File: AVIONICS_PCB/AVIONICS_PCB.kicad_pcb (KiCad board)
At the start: 2 copper layers, 5 parts, among them U1 ESP32-S3-DevKitC

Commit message: Added power system
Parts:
- added C1: C, Capacitor_SMD:C_0805_2012Metric_Pad1.18x1.45mm_HandSolder, F.Cu at (128.9, 81.0)
- added CR1: LD1117V33, LD1117V33:TO-220_STM, F.Cu at (131.5, 84.5)
- added J1: XT30PW-M, XT30PW-M:AMASS_XT30PW-M, F.Cu at (129.0, 66.7)
- moved SD_READER1 94.6 mm to (102.5, 119.0)
- moved GPS1 39.1 mm to (173.9, 66.0)
- moved ACCELEROMETER1 37.1 mm to (99.0, 80.7)
- moved ALTITUDE1 8.63 mm to (107.0, 89.2)
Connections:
- U1 pad 42: RX -> TX
- U1 pad 43: TX -> RX
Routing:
- net TX: track 0.00 -> 22.9 mm
- net RX: track 0.00 -> 20.9 mm
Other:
- board outline added: 103.5 x 77 mm

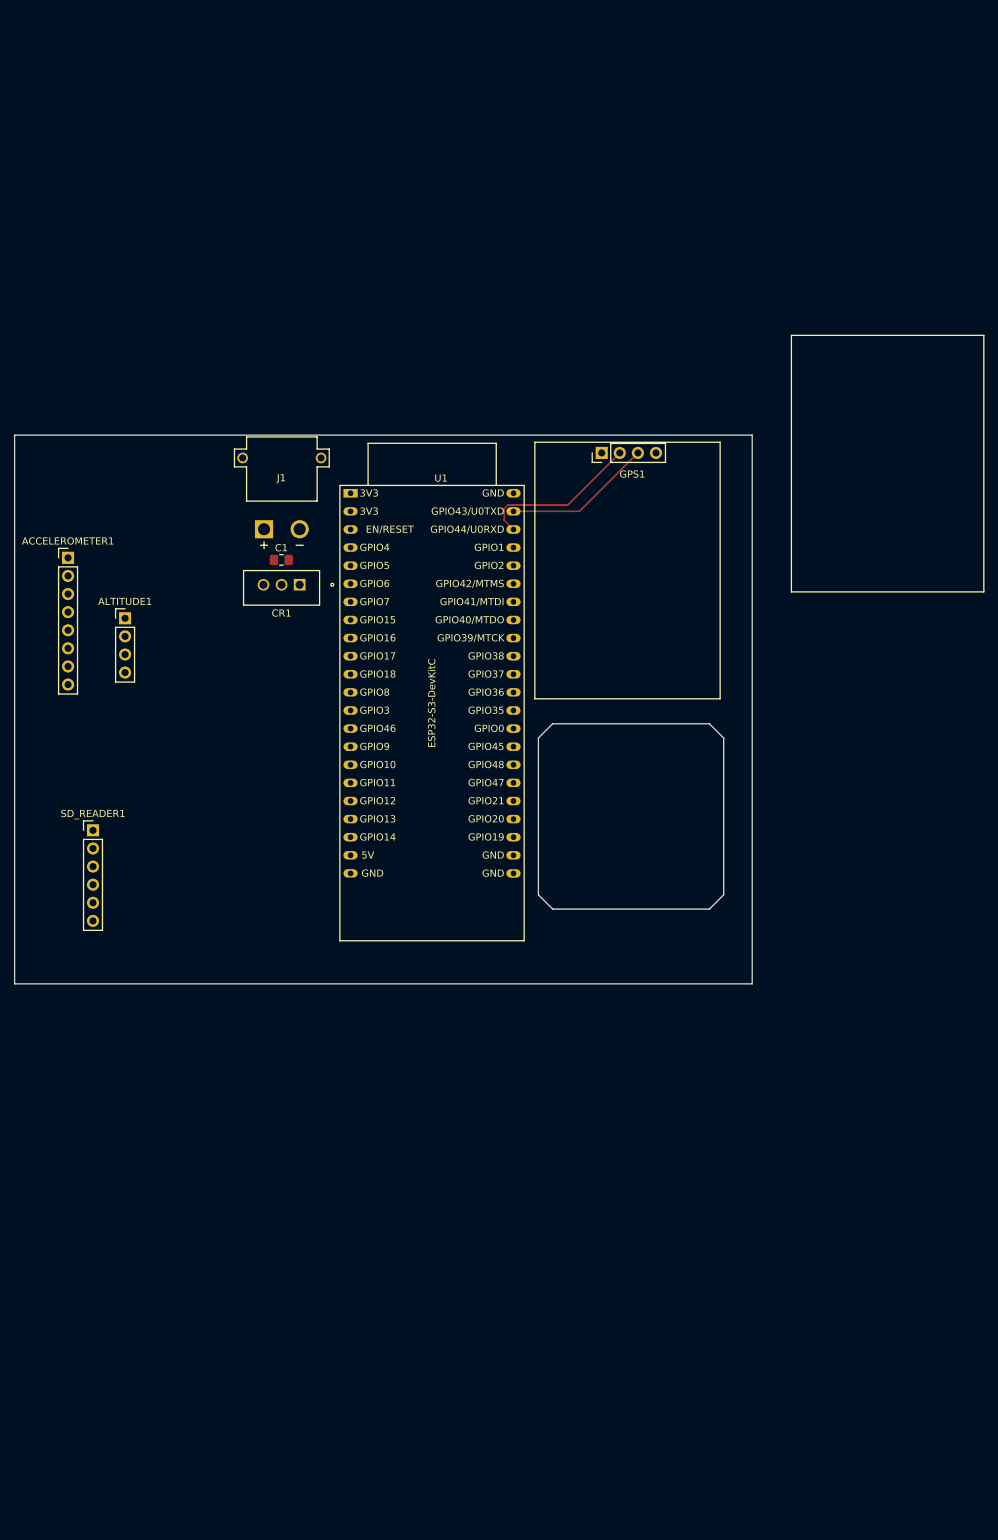
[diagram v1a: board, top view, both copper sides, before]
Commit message: Got sensors in right configuration
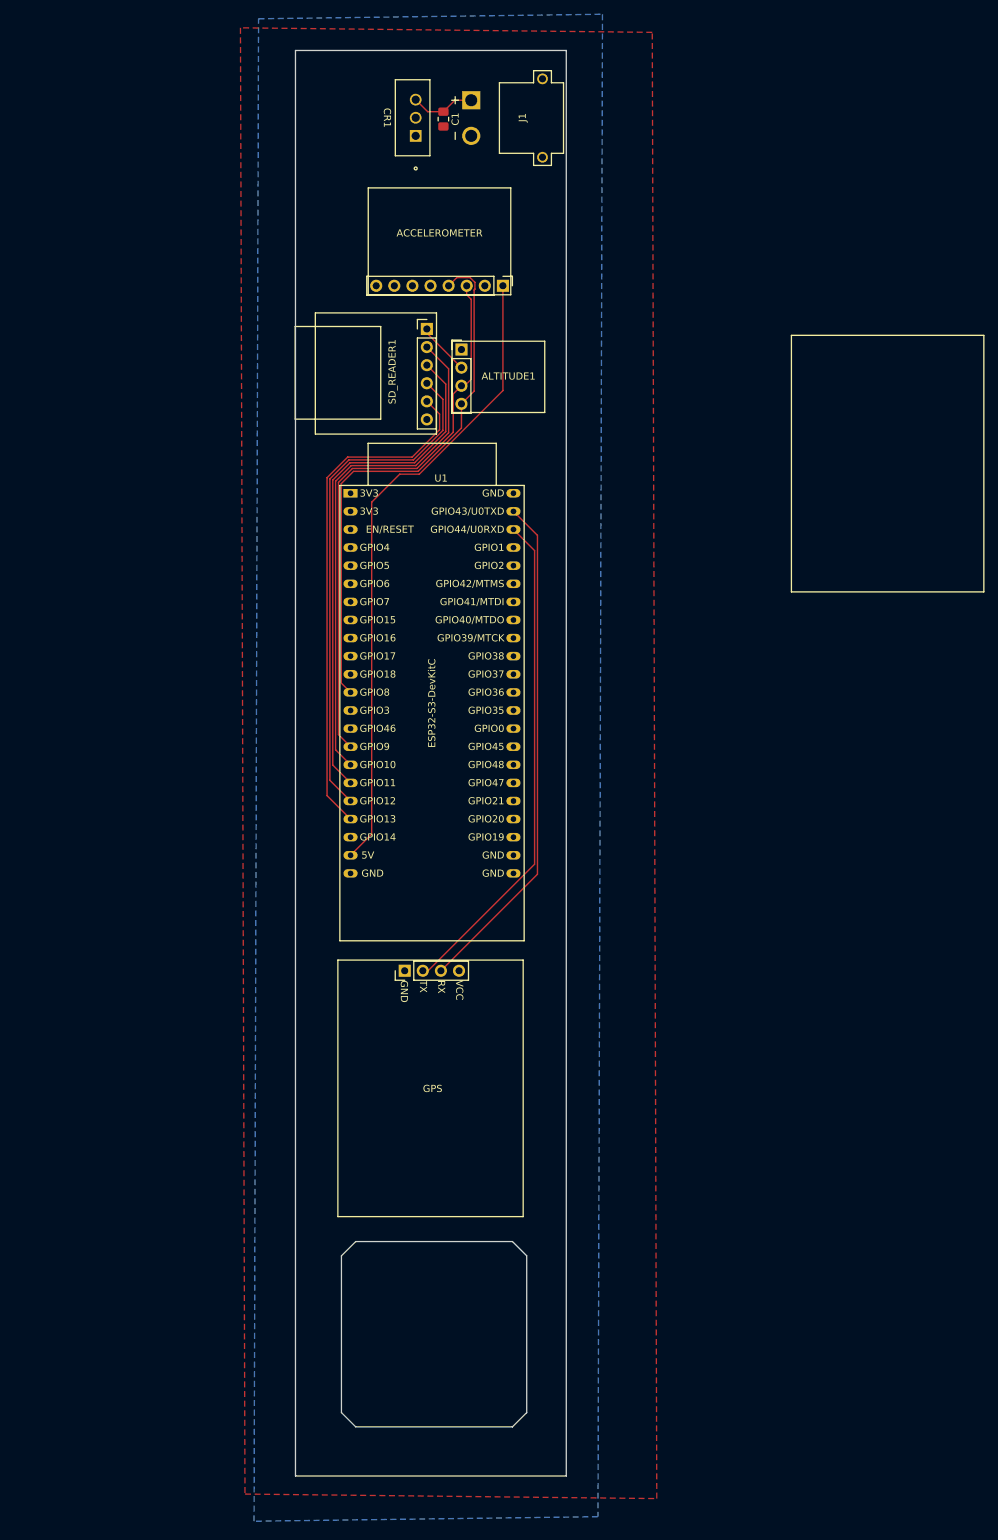
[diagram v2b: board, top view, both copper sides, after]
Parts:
- moved SD_READER1 84.5 mm to (149.3, 48.6)
- moved GPS 77.7 mm to (146.2, 138.7)
- moved ACCELEROMETER 72.0 mm to (160.0, 42.5), turned to -90 degrees
- moved C1 65.9 mm to (151.7, 19.2), turned to -90 degrees
- moved CR1 65.1 mm to (147.8, 21.5), turned to 90 degrees
- moved ALTITUDE1 60.4 mm to (154.2, 51.5)
- moved J1 60.1 mm to (165.6, 19.0), turned to -90 degrees
- renumbered ACCELEROMETER1 to ACCELEROMETER, GPS1 to GPS
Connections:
- GPS pad 4: +5V -> +3V3
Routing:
- net +5V: track 0.00 -> 90.4 mm
- net SCL: track 0.00 -> 78.9 mm
- net SDA: track 0.00 -> 75.6 mm
- net MOSI: track 0.00 -> 72.6 mm
- net CS: track 0.00 -> 72.6 mm
- net CLK: track 0.00 -> 72.6 mm
- net MISO: track 0.00 -> 72.6 mm
- net RX: track 20.9 -> 71.5 mm
- net TX: track 22.9 -> 70.1 mm
- net Net-(CR1-VIN): track 0.00 -> 9.16 mm
- net GND: track 0.00 -> 7.44 mm
- added copper zone on B.Cu, net +3V3
- added copper zone on F.Cu, net GND
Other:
- board size 103.5 x 77 mm -> 38 x 200 mm
- board text added: "GND"
- board text added: "RX"
- board text added: "TX"
- board text added: "VCC"

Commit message: Compact the board
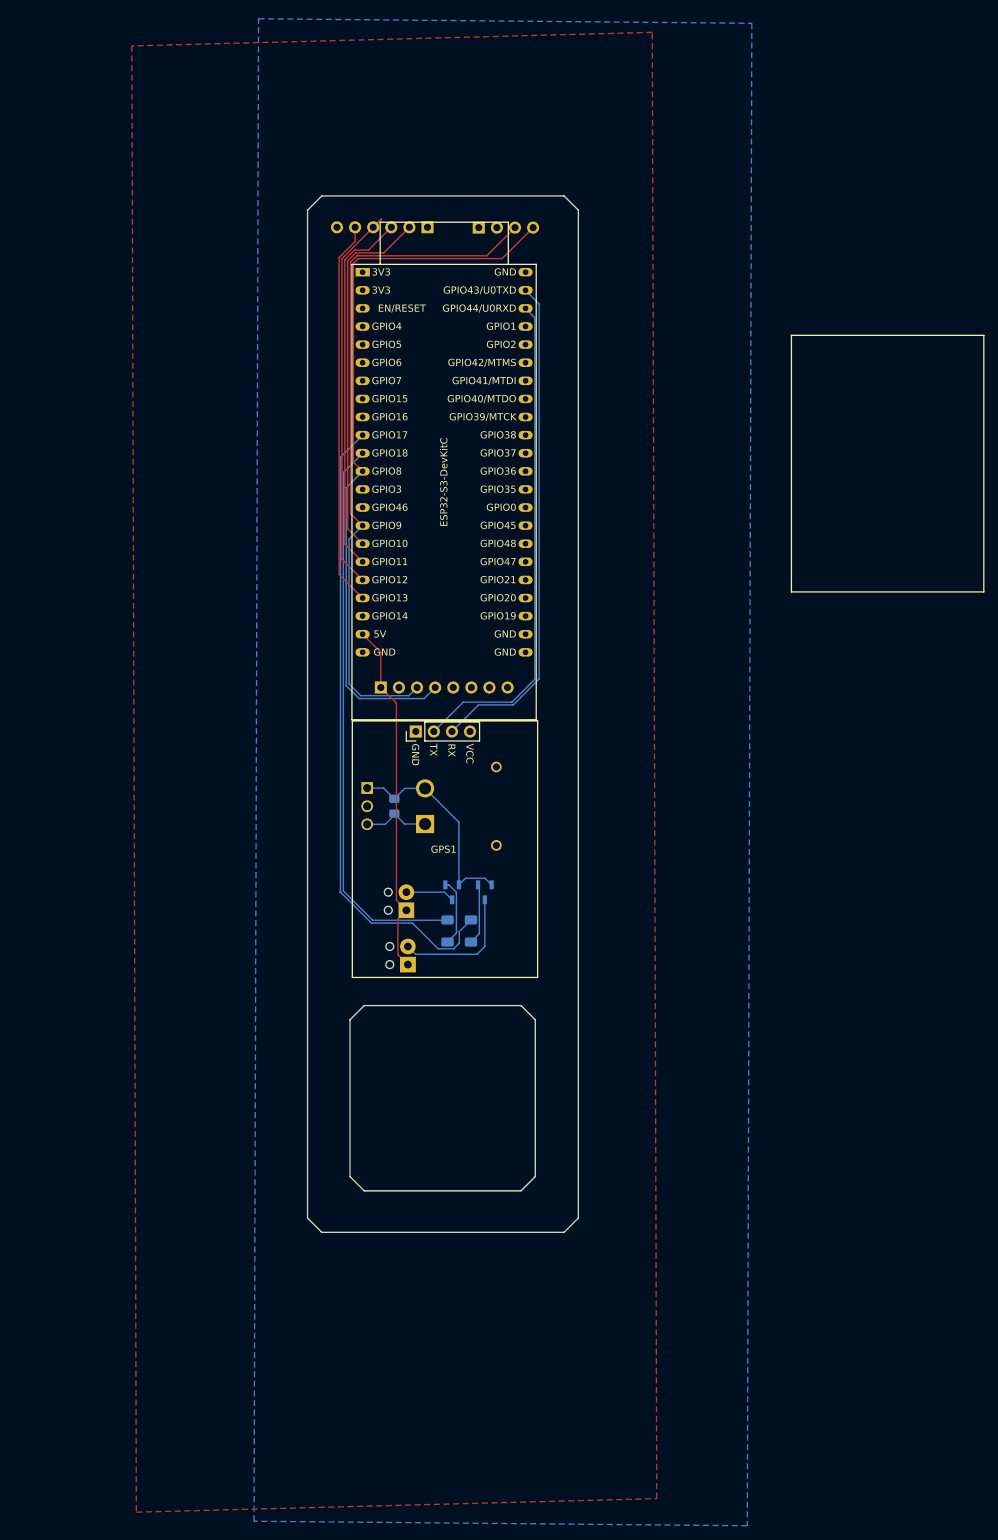
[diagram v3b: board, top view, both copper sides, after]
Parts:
- added IC1: MMBT2222ALT1G, SamacSys_Parts:SOT96P237X111-3N, B.Cu at (152.9, 127.7)
- added IC2: MMBT2222ALT1G, SamacSys_Parts:SOT96P237X111-3N, B.Cu at (157.5, 127.7)
- added J2: Screw_Terminal_01x02, TerminalBlock_Phoenix:TerminalBlock_Phoenix_MPT-0,5-2-2.54_1x02_P2.54mm_Horizontal, B.Cu at (146.5, 130.2)
- added J3: Screw_Terminal_01x02, TerminalBlock_Phoenix:TerminalBlock_Phoenix_MPT-0,5-2-2.54_1x02_P2.54mm_Horizontal, B.Cu at (146.7, 137.8)
- added R1: R_US, Resistor_SMD:R_1206_3216Metric_Pad1.30x1.75mm_HandSolder, B.Cu at (152.2, 133.1)
- added R2: R_US, Resistor_SMD:R_1206_3216Metric_Pad1.30x1.75mm_HandSolder, B.Cu at (155.5, 133.1)
- ACCELEROMETER1: renamed from ACCELEROMETER; moved to B.Cu
- ALTITUDE1, C1, CR1, J1, SD_READER1: moved to B.Cu
- moved J1 96.8 mm to (159.1, 115.6), turned to 90 degrees
- moved C1 96.7 mm to (144.8, 115.6), turned to 90 degrees
- moved CR1 91.8 mm to (141.0, 113.0), turned to -90 degrees
- moved ACCELEROMETER1 58.9 mm to (142.9, 98.9)
- moved GPS1 33.6 mm to (147.8, 105.1)
- moved U1 31.1 mm to (140.3, 40.6)
- moved ALTITUDE1 17.3 mm to (156.6, 34.4), turned to -90 degrees
- moved SD_READER1 14.3 mm to (149.4, 34.3), turned to 90 degrees
- renumbered GPS to GPS1
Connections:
- U1 pad 10: unconnected-(U1-GPIO17/ADC2_CH6-Pad10) -> Parachute2
- U1 pad 11: unconnected-(U1-GPIO18/ADC2_CH7-Pad11) -> Parachute1
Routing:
- net Parachute2: track 0.00 -> 89.7 mm
- net Parachute1: track 0.00 -> 78.9 mm
- net +5V: track 90.4 -> 50.0 mm
- net SDA: track 75.6 -> 101.9 mm
- net GND: track 7.44 -> 30.2 mm
- net CS: track 72.6 -> 51.2 mm
- net MOSI: track 72.6 -> 51.8 mm
- net Net-(IC2-C): track 0.00 -> 18.3 mm
- net MISO: track 72.6 -> 54.3 mm
- net SCL: track 78.9 -> 96.5 mm
- net CLK: track 72.6 -> 55.8 mm
- net Net-(IC1-B): track 0.00 -> 9.48 mm
- net Net-(IC2-B): track 0.00 -> 8.59 mm
- net Net-(IC1-C): track 0.00 -> 6.86 mm
- net RX: track 71.5 -> 70.6 mm
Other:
- board size 38 x 200 mm -> 38 x 145.4 mm
- board text added: "CLK"
- board text added: "CS"
- board text added: "MISO"
- board text added: "MOSI"
- board text added: "SCL"
- board text added: "SDA"
- board text added: "VNN"

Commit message: Board v2
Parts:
- added C2: C, Capacitor_SMD:C_0805_2012Metric_Pad1.18x1.45mm_HandSolder, B.Cu at (144.5, 54.0)
- added C3: C, Capacitor_SMD:C_0805_2012Metric_Pad1.18x1.45mm_HandSolder, B.Cu at (144.5, 57.0)
- added C4: C, Capacitor_SMD:C_0805_2012Metric_Pad1.18x1.45mm_HandSolder, B.Cu at (144.5, 60.0)
- added C5: C, Capacitor_SMD:C_0805_2012Metric_Pad1.18x1.45mm_HandSolder, B.Cu at (144.5, 63.0)
- added G***: LOGO, LOGO, F.Cu at (160.0, 127.6)
- added J4: Conn_01x03, Connector_Molex:Molex_KK-254_AE-6410-03A_1x03_P2.54mm_Vertical, B.Cu at (154.3, 56.5)
- added J5: Conn_01x03, Connector_Molex:Molex_KK-254_AE-6410-03A_1x03_P2.54mm_Vertical, B.Cu at (154.3, 64.3)
- added J6: Conn_01x03, Connector_Molex:Molex_KK-254_AE-6410-03A_1x03_P2.54mm_Vertical, B.Cu at (154.3, 72.2)
- added J7: Conn_01x03, Connector_Molex:Molex_KK-254_AE-6410-03A_1x03_P2.54mm_Vertical, B.Cu at (154.3, 80.0)
- renumbered ACCELEROMETER1 to ACCELEROMETER, ALTITUDE1 to ALTITUDE, GPS1 to GPS, SD_READER1 to SD_READER
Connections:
- J1 pad S1: (no net) -> GND
- J1 pad S2: (no net) -> GND
- J2 pad 1: +5V -> +3V3
- J3 pad 1: +5V -> +3V3
- U1 pad 32: unconnected-(U1-GPIO35-Pad32) -> servo4
- U1 pad 33: unconnected-(U1-GPIO36-Pad33) -> servo3
- U1 pad 34: unconnected-(U1-GPIO37-Pad34) -> servo2
- U1 pad 35: unconnected-(U1-GPIO38-Pad35) -> servo1
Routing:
- net +5V: track 50.0 -> 8.54 mm
- net GND: track 30.2 -> 52.9 mm
- net servo4: track 0.00 -> 12.6 mm
- net servo1: track 0.00 -> 11.8 mm
- net servo3: track 0.00 -> 10.4 mm
- net servo2: track 0.00 -> 9.61 mm
- net +3V3: track 0.00 -> 8.85 mm
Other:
- board size 38 x 145.4 mm -> 38 x 109.8 mm
- board text added: "Authors: Alex B, Sawyer, Brandon"
- board text added: "Rocket Avionics Board V2"

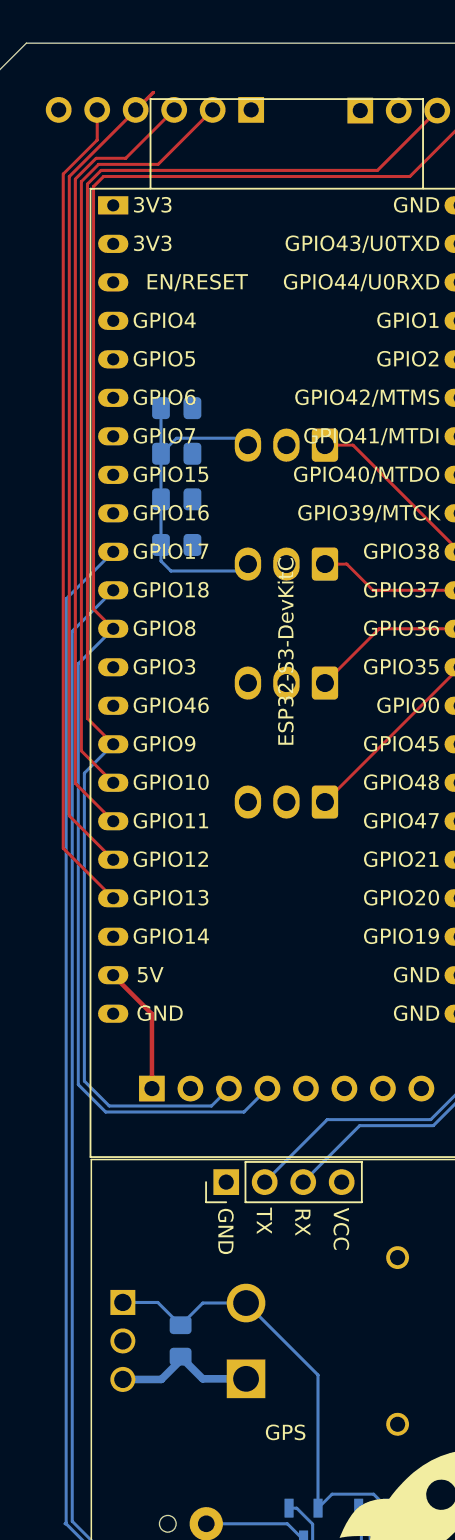
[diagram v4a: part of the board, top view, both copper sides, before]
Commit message: added SD card
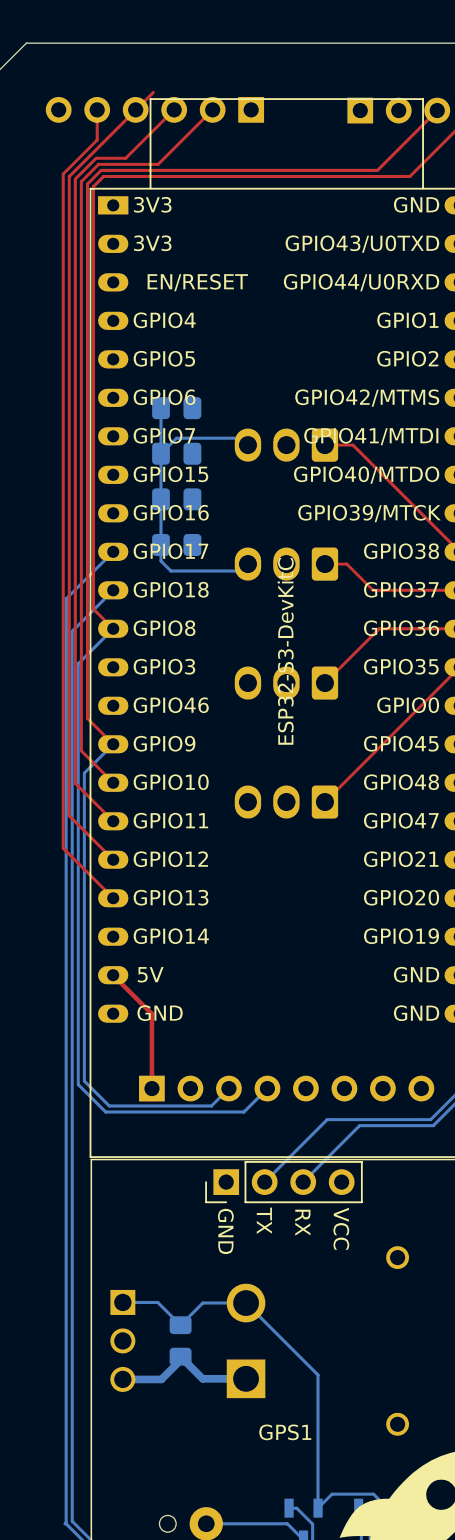
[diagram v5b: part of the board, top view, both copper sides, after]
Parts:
- renumbered ACCELEROMETER to ACCELEROMETER1, ALTITUDE to ALTITUDE1, GPS to GPS1, SD_READER to SD_READER1
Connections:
- SD_READER1 pad 2: CS -> MISO
- SD_READER1 pad 3: MOSI -> CLK
- SD_READER1 pad 4: CLK -> MOSI
- SD_READER1 pad 5: MISO -> CS
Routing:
- net CLK: track 55.8 -> 54.1 mm
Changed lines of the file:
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@@
 		(descr "Through hole straight pin header, 1x04, 2.54mm pitch, single row")
 		(tags "Through hole pin header THT 1x04 2.54mm single row")
-		(property "Reference" "GPS"
+		(property "Reference" "GPS1"
 			(at -16.55 3.92 0)
 			(layer "F.SilkS")
@@
 			(at 0 0 90)
 			(layer "B.SilkS")
-			(hide yes)
 			(effects
 				(font
@@
 			(at 0 0 90)
 			(layer "B.SilkS")
-			(hide yes)
 			(effects
 				(font
@@
 		(descr "Through hole straight pin header, 1x06, 2.54mm pitch, single row")
 		(tags "Through hole pin header THT 1x06 2.54mm single row")
-		(property "Reference" "SD_READER"
+		(property "Reference" "SD_READER1"
 			(at -7.740817 -6.006849 0)
 			(layer "B.SilkS")
@@
 			(layers "*.Cu" "*.Mask")
 			(remove_unused_layers no)
-			(net 12 "CS")
+			(net 15 "MISO")
 			(pinfunction "Pin_2")
 			(pintype "passive")
@@
 			(layers "*.Cu" "*.Mask")
 			(remove_unused_layers no)
-			(net 13 "MOSI")
+			(net 14 "CLK")
 			(pinfunction "Pin_3")
 			(pintype "passive")
@@
 			(layers "*.Cu" "*.Mask")
 			(remove_unused_layers no)
-			(net 14 "CLK")
+			(net 13 "MOSI")
 			(pinfunction "Pin_4")
 			(pintype "passive")
@@
 			(layers "*.Cu" "*.Mask")
 			(remove_unused_layers no)
-			(net 15 "MISO")
+			(net 12 "CS")
 			(pinfunction "Pin_5")
 			(pintype "passive")
@@
 		(descr "Through hole straight pin header, 1x08, 2.54mm pitch, single row")
 		(tags "Through hole pin header THT 1x08 2.54mm single row")
-		(property "Reference" "ACCELEROMETER"
+		(property "Reference" "ACCELEROMETER1"
 			(at -7.383017 -8.89 0)
 			(layer "B.SilkS")
@@
 		(descr "Through hole straight pin header, 1x04, 2.54mm pitch, single row")
 		(tags "Through hole pin header THT 1x04 2.54mm single row")
-		(property "Reference" "ALTITUDE"
+		(property "Reference" "ALTITUDE1"
 			(at 8.255 -3.751729 90)
 			(layer "B.SilkS")
@@
 	)
 	(gr_text "MOSI"
-		(at 143.915001 39.54 -90)
+		(at 140.97 39.54 -90)
 		(layer "B.SilkS")
 		(effects
@@
 	)
 	(gr_text "CLK"
-		(at 141.375001 38.905 -90)
+		(at 143.51 38.735 -90)
 		(layer "B.SilkS")
 		(effects
@@
 	)
 	(gr_text "CS"
-		(at 146.455001 38.27 -90)
+		(at 138.600714 37.897143 -90)
 		(layer "B.SilkS")
 		(effects
@@
 	)
 	(gr_text "MISO"
-		(at 138.835001 39.54 -90)
+		(at 146.256678 39.537749 -90)
 		(layer "B.SilkS")
 		(effects
@@
 	)
 	(segment
-		(start 142.96685 33.189183)
-		(end 142.983073 33.189183)
-		(width 0.2)
-		(layer "F.Cu")
-		(net 14)
-	)
-	(segment
 		(start 137.435 80.92)
 		(end 140.335 83.82)
 		(width 0.2)
 		(layer "F.Cu")
-		(net 14)
-	)
-	(segment
-		(start 141.81685 34.339183)
-		(end 142.96685 33.189183)
-		(width 0.2)
-		(layer "F.Cu")
